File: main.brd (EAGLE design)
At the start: 30.5 x 12.7 mm, 8 parts

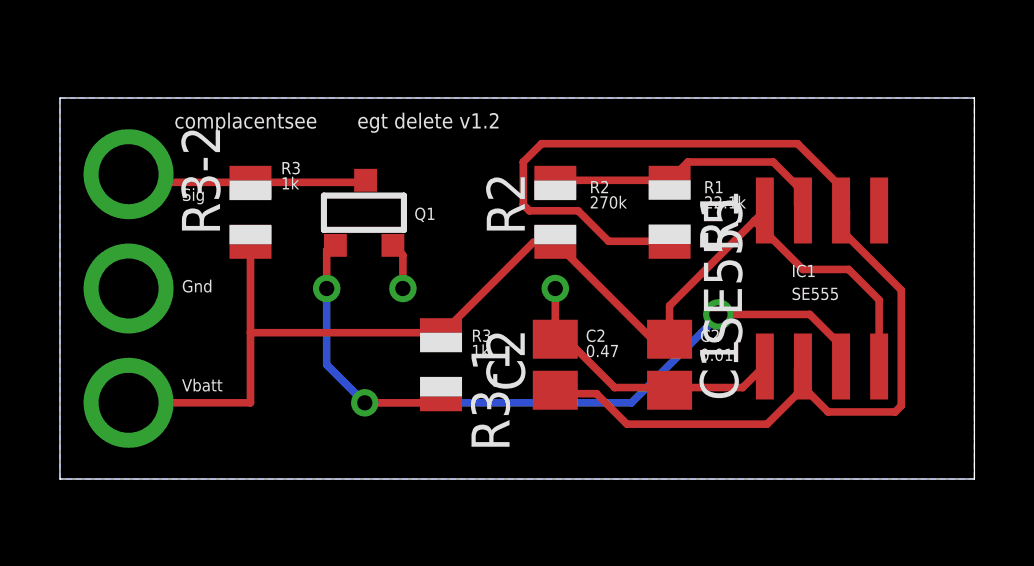
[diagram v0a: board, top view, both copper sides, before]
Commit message: Corrections for pads
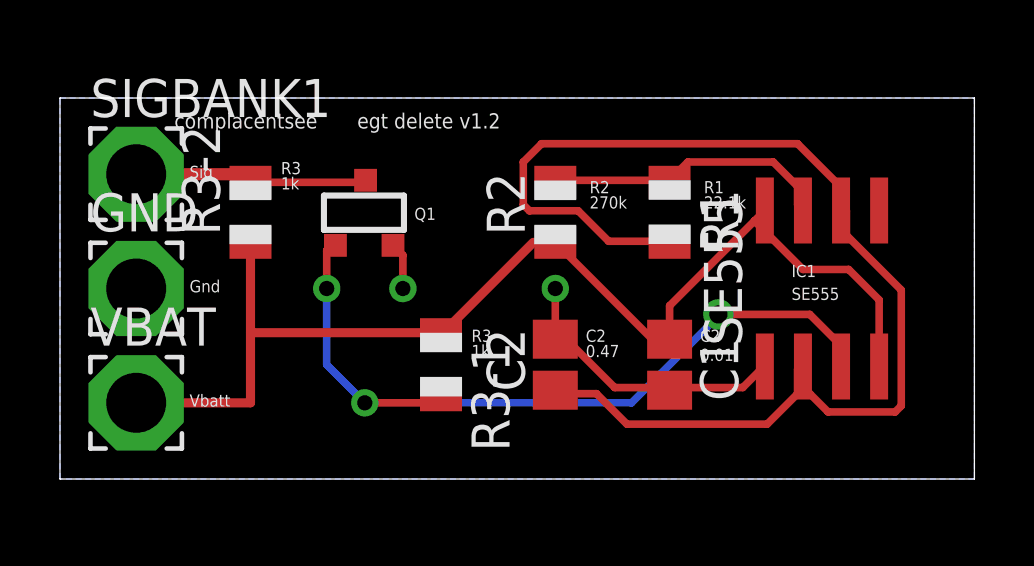
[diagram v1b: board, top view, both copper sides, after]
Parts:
- added GND: GND, wirepad:3,17/1,3
- added SIGBANK1: SIGBANK1, wirepad:3,17/1,3
- added VBAT: (no value), wirepad:3,17/1,3
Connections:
- net GND: now also GND.1
- net SIGBANK1: now also SIGBANK1.1
- net VBAT: now also VBAT.1
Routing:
- net SIGBANK1: track 8.20 -> 7.94 mm, vias 1 -> 0
- net VBAT: vias 1 -> 0
- net GND: vias 3 -> 2
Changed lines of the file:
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@@
 <layers>
 <layer number="1" name="Top" color="4" fill="1" visible="yes" active="yes"/>
+<layer number="2" name="Route2" color="1" fill="3" visible="no" active="no"/>
+<layer number="3" name="Route3" color="4" fill="3" visible="no" active="no"/>
+<layer number="14" name="Route14" color="1" fill="6" visible="no" active="no"/>
+<layer number="15" name="Route15" color="4" fill="6" visible="no" active="no"/>
 <layer number="16" name="Bottom" color="1" fill="1" visible="yes" active="yes"/>
 <layer number="17" name="Pads" color="2" fill="1" visible="yes" active="yes"/>
@@
 <wire x1="30.48" y1="12.7" x2="0" y2="12.7" width="0" layer="20"/>
 <wire x1="0" y1="12.7" x2="0" y2="0" width="0" layer="20"/>
-<text x="4.064" y="9.271" size="0.4064" layer="21" font="vector" ratio="15">Sig</text>
-<text x="4.064" y="6.223" size="0.4064" layer="21" font="vector" ratio="15">Gnd</text>
-<text x="4.064" y="2.921" size="0.4064" layer="21" font="vector" ratio="15">Vbatt</text>
+<text x="4.318" y="10.033" size="0.4064" layer="21" font="vector" ratio="15">Sig</text>
+<text x="4.318" y="6.223" size="0.4064" layer="21" font="vector" ratio="15">Gnd</text>
+<text x="4.318" y="2.413" size="0.4064" layer="21" font="vector" ratio="15">Vbatt</text>
 <text x="17.653" y="9.525" size="0.4064" layer="21" font="vector" ratio="15">R2</text>
 <text x="17.653" y="9.017" size="0.4064" layer="21" font="vector" ratio="15">270k</text>
@@
 <element name="C2" library="adafruit" package="C0805" value=".47u" x="16.51" y="3.81" rot="R90"/>
 <element name="C1" library="adafruit" package="C0805" value="0.01u" x="20.32" y="3.81" rot="R270"/>
+<element name="VBAT" library="wirepad" package="3,17/1,3" value="" x="2.54" y="2.54"/>
+<element name="GND" library="wirepad" package="3,17/1,3" value="GND" x="2.54" y="6.35"/>
+<element name="SIGBANK1" library="wirepad" package="3,17/1,3" value="SIGBANK1" x="2.54" y="10.16"/>
 </elements>
 <signals>
@@
 <contactref element="SE555" pad="4"/>
 <wire x1="12.5984" y1="4.8768" x2="12.7" y2="4.81" width="0.254" layer="1"/>
-<wire x1="12.7" y1="4.81" x2="15.78" y2="7.89" width="0.254" layer="1"/>
+<wire x1="12.7" y1="4.81" x2="15.78" y2="7.89" width="0.3048" layer="1"/>
 <wire x1="15.78" y1="7.89" x2="16.51" y2="7.89" width="0.254" layer="1"/>
 <wire x1="16.51" y1="7.89" x2="19.74" y2="4.66" width="0.254" layer="1"/>
@@
 <wire x1="24.765" y1="6.985" x2="26.289" y2="6.985" width="0.254" layer="1"/>
 <wire x1="23.1475" y1="8.6025" x2="24.765" y2="6.985" width="0.254" layer="1"/>
-<wire x1="6.35" y1="4.8768" x2="6.35" y2="7.89" width="0.254" layer="1"/>
-<wire x1="6.35" y1="4.8768" x2="12.5984" y2="4.8768" width="0.254" layer="1"/>
-<via x="2.286" y="2.54" extent="1-16" drill="2" shape="square"/>
-<wire x1="6.35" y1="4.8768" x2="6.35" y2="2.54" width="0.254" layer="1"/>
-<wire x1="6.35" y1="2.54" x2="2.286" y2="2.54" width="0.254" layer="1"/>
+<wire x1="6.35" y1="4.8768" x2="6.35" y2="7.89" width="0.3048" layer="1"/>
+<wire x1="6.35" y1="4.8768" x2="12.5984" y2="4.8768" width="0.3048" layer="1"/>
+<wire x1="6.35" y1="4.8768" x2="6.35" y2="2.54" width="0.3048" layer="1"/>
+<wire x1="6.35" y1="2.54" x2="2.286" y2="2.54" width="0.3048" layer="1"/>
+<contactref element="VBAT" pad="1"/>
+<wire x1="2.286" y1="2.54" x2="2.54" y2="2.54" width="0" layer="19" extent="1-1"/>
 </signal>
 <signal name="GND">
@@
 <vertex x="0" y="0"/>
 </polygon>
-<via x="2.286" y="6.35" extent="1-16" drill="2" shape="square"/>
+<contactref element="GND" pad="1"/>
 </signal>
 <signal name="SIGBANK1">
@@
 <wire x1="6.35" y1="9.89" x2="10.1186" y2="9.89" width="0.254" layer="1"/>
 <wire x1="10.1186" y1="9.89" x2="10.1854" y2="9.9568" width="0.254" layer="1"/>
-<via x="2.286" y="10.16" extent="1-16" drill="2" shape="square"/>
-<wire x1="6.35" y1="9.89" x2="2.286" y2="9.89" width="0.254" layer="1"/>
-<wire x1="2.286" y1="9.89" x2="2.286" y2="10.16" width="0.254" layer="1"/>
+<contactref element="SIGBANK1" pad="1"/>
+<wire x1="2.54" y1="10.16" x2="6.35" y2="10.16" width="0.4064" layer="1"/>
+<wire x1="6.35" y1="10.16" x2="6.35" y2="9.89" width="0.4064" layer="1"/>
 </signal>
 <signal name="DIS">
@@
 </signal>
 </signals>
+<errors>
+</errors>
 </board>
 </drawing>
